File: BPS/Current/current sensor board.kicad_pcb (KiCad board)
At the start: 2 copper layers, 74.9 x 52.1 mm, 45 parts, among them J1 Connector_Generic:Conn_01x04, U1 REF5040ADGK, U2 RecomRB-0515D, U3 L08P50, U4 L08P100, U5 OPA4376

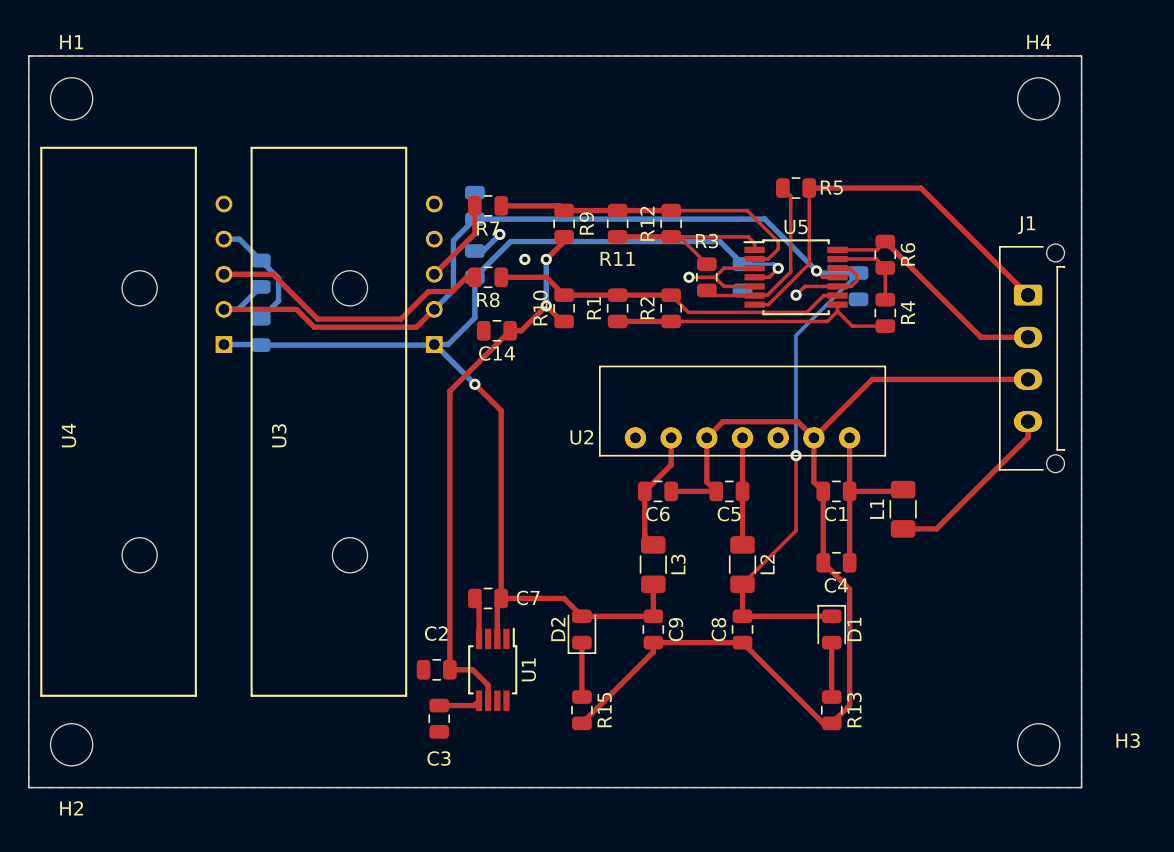
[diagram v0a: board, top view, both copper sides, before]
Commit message: Move connector and round corners, generate gerbers
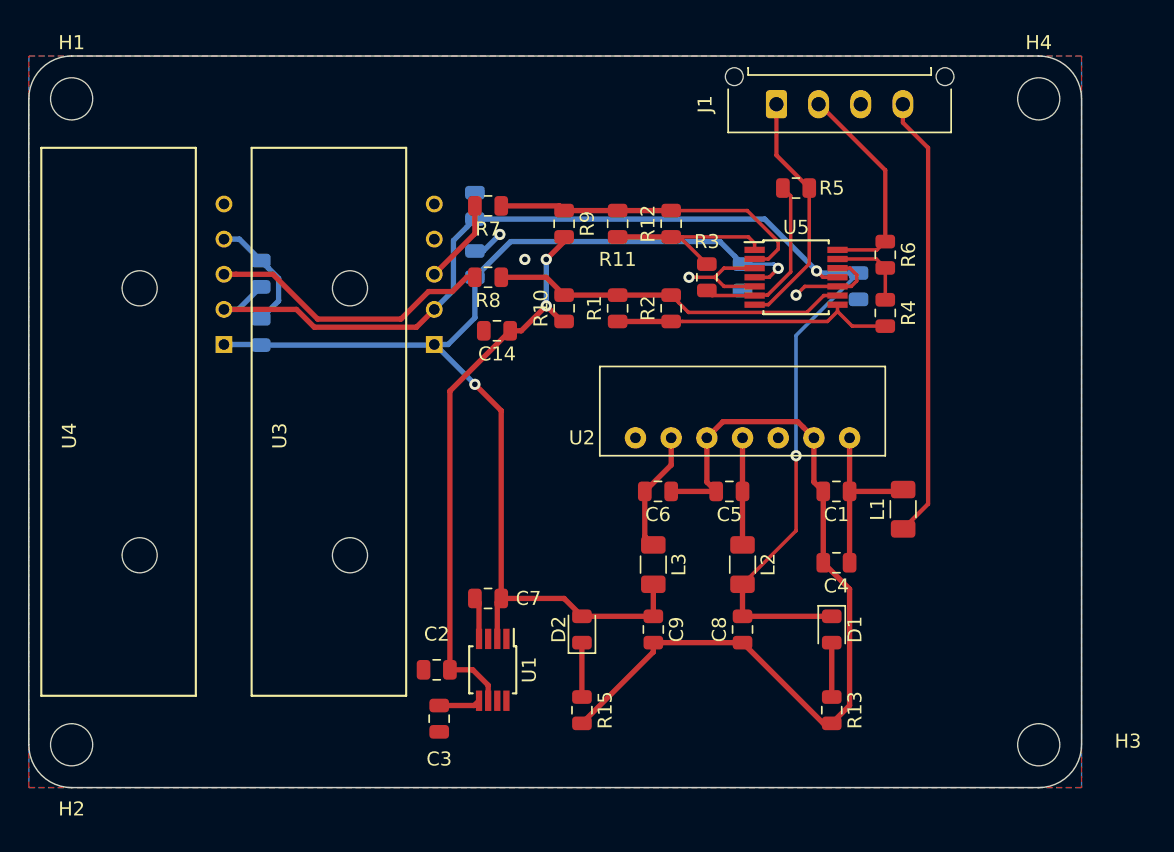
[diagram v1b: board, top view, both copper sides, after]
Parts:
- moved J1 22.5 mm to (135.8, 62.6), turned to 0 degrees
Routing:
- net +5V: track 12.7 -> 31.7 mm
- net GND: track 106.1 -> 89.2 mm
- net /LOW_OUT: track 29.2 -> 17.4 mm
- net /HIGH_OUT: track 16.6 -> 15.4 mm
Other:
- outline, holes or cut-outs redrawn
- rule trace_min: 0.2 -> 0.1
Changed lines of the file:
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@@
-(kicad_pcb (version 20171130) (host pcbnew 5.1.4-e60b266~84~ubuntu19.04.1)
+(kicad_pcb (version 20171130) (host pcbnew "(5.0.0)")
   (general
     (thickness 1.6)
     (drawings 8)
-    (tracks 191)
+    (tracks 190)
     (zones 0)
     (modules 45)
@@
   )
   (setup
-    (last_trace_width 0.381)
+    (last_trace_width 0.1)
+    (user_trace_width 0.1)
     (user_trace_width 0.2032)
     (user_trace_width 0.254)
@@
     (zone_clearance 0.508)
     (zone_45_only no)
-    (trace_min 0.2)
+    (trace_min 0.1)
+    (segment_width 0.2)
+    (edge_width 0.1)
     (via_size 0.8)
     (via_drill 0.4)
@@
     (uvia_min_size 0.2)
     (uvia_min_drill 0.1)
-    (edge_width 0.1)
-    (segment_width 0.2)
     (pcb_text_width 0.3)
     (pcb_text_size 1.5 1.5)
@@
     (pad_to_mask_clearance 0)
     (aux_axis_origin 0 0)
-    (visible_elements FFFFFF7F)
+    (visible_elements 7FFFFFFF)
     (pcbplotparams
       (layerselection 0x010fc_ffffffff)
@@
     (add_net "Net-(R7-Pad2)")
     (add_net "Net-(R8-Pad2)")
-    (add_net "Net-(U1-Pad1)")
-    (add_net "Net-(U1-Pad3)")
-    (add_net "Net-(U1-Pad7)")
-    (add_net "Net-(U1-Pad8)")
-    (add_net "Net-(U3-Pad5)")
-    (add_net "Net-(U4-Pad5)")
   )
   (module MountingHole:MountingHole_3mm (layer F.Cu)
@@
   )
   (module Connector_Molex:Molex_Micro-Fit_3.0_43650-0415_1x04_P3.00mm_Vertical (layer F.Cu)
-    (at 153.67 76.2 270)
+    (at 135.763 62.611)
     (descr "Molex Micro-Fit 3.0 Connector System, 43650-0415 (compatible alternatives: 43650-0416, 43650-0417), 4 Pins per row (http://www.molex.com/pdm_docs/sd/436500215_sd.pdf), generated with kicad-footprint-generator")
     (tags "connector Molex Micro-Fit_3.0 vertical")
-    (fp_text reference J1 (at -5.08 0 180) (layer F.SilkS)
-      (effects (font (size 1 1) (thickness 0.15)))
-    )
-    (fp_text value Connector_Generic:Conn_01x04 (at 4.5 4.5 90) (layer F.Fab)
-      (effects (font (size 1 1) (thickness 0.15)))
-    )
-    (fp_text user %R (at 4.5 1.2 90) (layer F.Fab)
+    (fp_text reference J1 (at -5.08 0 -90) (layer F.SilkS)
+      (effects (font (size 1 1) (thickness 0.15)))
+    )
+    (fp_text value Connector_Generic:Conn_01x04 (at 4.5 4.5 -180) (layer F.Fab)
+      (effects (font (size 1 1) (thickness 0.15)))
+    )
+    (fp_text user %R (at 4.5 1.2 -180) (layer F.Fab)
       (effects (font (size 1 1) (thickness 0.15)))
     )
@@
     (fp_line (start -2.125 -2.47) (end -3.325 -2.47) (layer F.Fab) (width 0.1))
     (fp_line (start -2.125 -1.97) (end -2.125 -2.47) (layer F.Fab) (width 0.1))
-    (pad 4 thru_hole oval (at 9 0 270) (size 1.5 2.02) (drill 1.02) (layers *.Cu *.Mask)
+    (pad 4 thru_hole oval (at 9 0) (size 1.5 2.02) (drill 1.02) (layers *.Cu *.Mask)
       (net 13 +5V))
-    (pad 3 thru_hole oval (at 6 0 270) (size 1.5 2.02) (drill 1.02) (layers *.Cu *.Mask)
-      (net 1 GND))
-    (pad 2 thru_hole oval (at 3 0 270) (size 1.5 2.02) (drill 1.02) (layers *.Cu *.Mask)
+    (pad 3 thru_hole oval (at 6 0) (size 1.5 2.02) (drill 1.02) (layers *.Cu *.Mask)
+      (net 1 GND))
+    (pad 2 thru_hole oval (at 3 0) (size 1.5 2.02) (drill 1.02) (layers *.Cu *.Mask)
       (net 12 /HIGH_OUT))
-    (pad 1 thru_hole roundrect (at 0 0 270) (size 1.5 2.02) (drill 1.02) (layers *.Cu *.Mask) (roundrect_rratio 0.166667)
+    (pad 1 thru_hole roundrect (at 0 0) (size 1.5 2.02) (drill 1.02) (layers *.Cu *.Mask) (roundrect_rratio 0.166667)
       (net 11 /LOW_OUT))
-    (pad "" np_thru_hole circle (at 12 -1.96 270) (size 1.27 1.27) (drill 1.27) (layers *.Cu *.Mask))
-    (pad "" np_thru_hole circle (at -3 -1.96 270) (size 1.27 1.27) (drill 1.27) (layers *.Cu *.Mask))
+    (pad "" np_thru_hole circle (at 12 -1.96) (size 1.27 1.27) (drill 1.27) (layers *.Cu *.Mask))
+    (pad "" np_thru_hole circle (at -3 -1.96) (size 1.27 1.27) (drill 1.27) (layers *.Cu *.Mask))
     (model ${KISYS3DMOD}/Connector_Molex.3dshapes/Molex_Micro-Fit_3.0_43650-0415_1x04_P3.00mm_Vertical.wrl
       (at (xyz 0 0 0))
@@
     )
   )
-  (gr_line (start 157.48 59.182) (end 157.48 59.69) (layer Edge.Cuts) (width 0.1))
-  (gr_line (start 82.55 59.182) (end 157.48 59.182) (layer Edge.Cuts) (width 0.1))
-  (gr_line (start 82.55 59.69) (end 82.55 59.182) (layer Edge.Cuts) (width 0.1))
-  (gr_line (start 157.48 111.252) (end 157.48 110.49) (layer Edge.Cuts) (width 0.1))
-  (gr_line (start 82.55 111.252) (end 157.48 111.252) (layer Edge.Cuts) (width 0.1))
-  (gr_line (start 82.55 110.49) (end 82.55 111.252) (layer Edge.Cuts) (width 0.1))
-  (gr_line (start 157.48 59.69) (end 157.48 110.49) (layer Edge.Cuts) (width 0.1))
-  (gr_line (start 82.55 110.49) (end 82.55 59.69) (layer Edge.Cuts) (width 0.1))
+  (gr_line (start 85.598 59.182) (end 154.432 59.182) (layer Edge.Cuts) (width 0.1))
+  (gr_line (start 82.55 108.204) (end 82.55 62.23) (layer Edge.Cuts) (width 0.1))
+  (gr_line (start 154.432 111.252) (end 85.598 111.252) (layer Edge.Cuts) (width 0.1))
+  (gr_line (start 157.48 62.23) (end 157.48 108.204) (layer Edge.Cuts) (width 0.1))
+  (gr_arc (start 154.432 62.23) (end 157.48 62.23) (angle -90) (layer Edge.Cuts) (width 0.1))
+  (gr_arc (start 154.432 108.204) (end 154.432 111.252) (angle -90) (layer Edge.Cuts) (width 0.1))
+  (gr_arc (start 85.598 108.204) (end 82.55 108.204) (angle -90) (layer Edge.Cuts) (width 0.1))
+  (gr_arc (start 85.598 62.23) (end 85.598 59.182) (angle -90) (layer Edge.Cuts) (width 0.1))
   (segment (start 97.5375 72.216) (end 99.06 73.7385) (width 0.381) (layer B.Cu) (net 1) (status 20))
   (segment (start 96.44 72.216) (end 97.5375 72.216) (width 0.381) (layer B.Cu) (net 1) (status 10))
@@
   (segment (start 137.668001 85.598001) (end 138.43 86.36) (width 0.381) (layer F.Cu) (net 1))
   (segment (start 130.81 86.36) (end 131.962501 85.207499) (width 0.381) (layer F.Cu) (net 1))
-  (segment (start 152.279 82.2) (end 153.67 82.2) (width 0.381) (layer F.Cu) (net 1) (status 20))
-  (segment (start 142.59 82.2) (end 152.279 82.2) (width 0.381) (layer F.Cu) (net 1))
-  (segment (start 138.43 86.36) (end 142.59 82.2) (width 0.381) (layer F.Cu) (net 1))
   (segment (start 139.7 106.68) (end 140.97 105.41) (width 0.381) (layer F.Cu) (net 1) (status 10))
   (segment (start 140.97 97.125) (end 139.095 95.25) (width 0.381) (layer F.Cu) (net 1) (status 20))
@@
   (segment (start 138.0975 73.9715) (end 135.189 76.88) (width 0.254) (layer F.Cu) (net 11))
   (segment (start 138.0975 68.58) (end 138.0975 73.9715) (width 0.254) (layer F.Cu) (net 11))
-  (segment (start 146.05 68.58) (end 138.0975 68.58) (width 0.381) (layer F.Cu) (net 11))
-  (segment (start 153.67 76.2) (end 146.05 68.58) (width 0.381) (layer F.Cu) (net 11))
+  (segment (start 135.763 66.2455) (end 138.0975 68.58) (width 0.3048) (layer F.Cu) (net 11))
+  (segment (start 135.763 62.611) (end 135.763 66.2455) (width 0.3048) (layer F.Cu) (net 11))
   (segment (start 142.92 72.98) (end 143.51 72.39) (width 0.254) (layer F.Cu) (net 12))
   (segment (start 140.11 72.98) (end 142.92 72.98) (width 0.254) (layer F.Cu) (net 12))
-  (segment (start 150.32 79.2) (end 143.51 72.39) (width 0.381) (layer F.Cu) (net 12))
-  (segment (start 153.67 79.2) (end 150.32 79.2) (width 0.381) (layer F.Cu) (net 12))
-  (segment (start 153.67 86.331) (end 153.67 85.2) (width 0.381) (layer F.Cu) (net 13) (status 20))
-  (segment (start 147.161 92.84) (end 153.67 86.331) (width 0.381) (layer F.Cu) (net 13))
-  (segment (start 144.78 92.84) (end 147.161 92.84) (width 0.381) (layer F.Cu) (net 13) (status 10))
+  (segment (start 138.811 62.611) (end 138.763 62.611) (width 0.3048) (layer F.Cu) (net 12))
+  (segment (start 143.51 72.39) (end 143.51 67.31) (width 0.3048) (layer F.Cu) (net 12))
+  (segment (start 143.51 67.31) (end 138.811 62.611) (width 0.3048) (layer F.Cu) (net 12))
+  (segment (start 144.78 92.84) (end 146.558 91.062) (width 0.3048) (layer F.Cu) (net 13))
+  (segment (start 144.763 63.9258) (end 144.763 62.611) (width 0.3048) (layer F.Cu) (net 13))
+  (segment (start 146.558 65.7208) (end 144.763 63.9258) (width 0.3048) (layer F.Cu) (net 13))
+  (segment (start 146.558 91.062) (end 146.558 65.7208) (width 0.3048) (layer F.Cu) (net 13))
   (segment (start 124.46 78.075) (end 128.27 78.075) (width 0.381) (layer F.Cu) (net 14))
   (segment (start 129.07 78.075) (end 128.27 78.075) (width 0.254) (layer F.Cu) (net 14))
